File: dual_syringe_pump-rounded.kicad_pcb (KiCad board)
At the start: 2 copper layers, 100.3 x 85.5 mm, 163 parts, among them J2 Barrel_Jack_Switch_Pin3Ring, Q1 SS8050, Q2 SS8050, Q3 SS8050, Q4 SS8050, U1 ESP32-WROOM-32, U2 AMS1117-3.3, U3 CH340C, U4 TP5100, U5 LM2596S-buck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

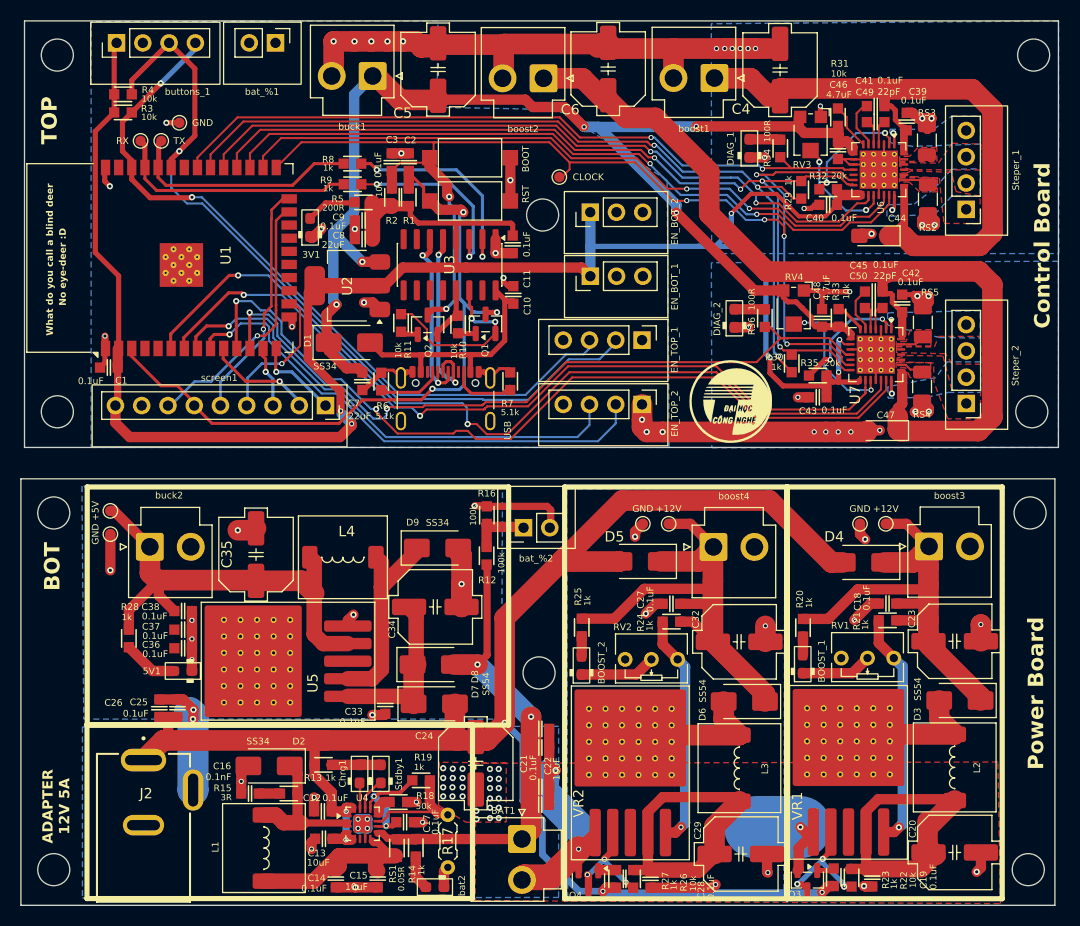
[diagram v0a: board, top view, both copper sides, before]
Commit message: Highlighted connectors
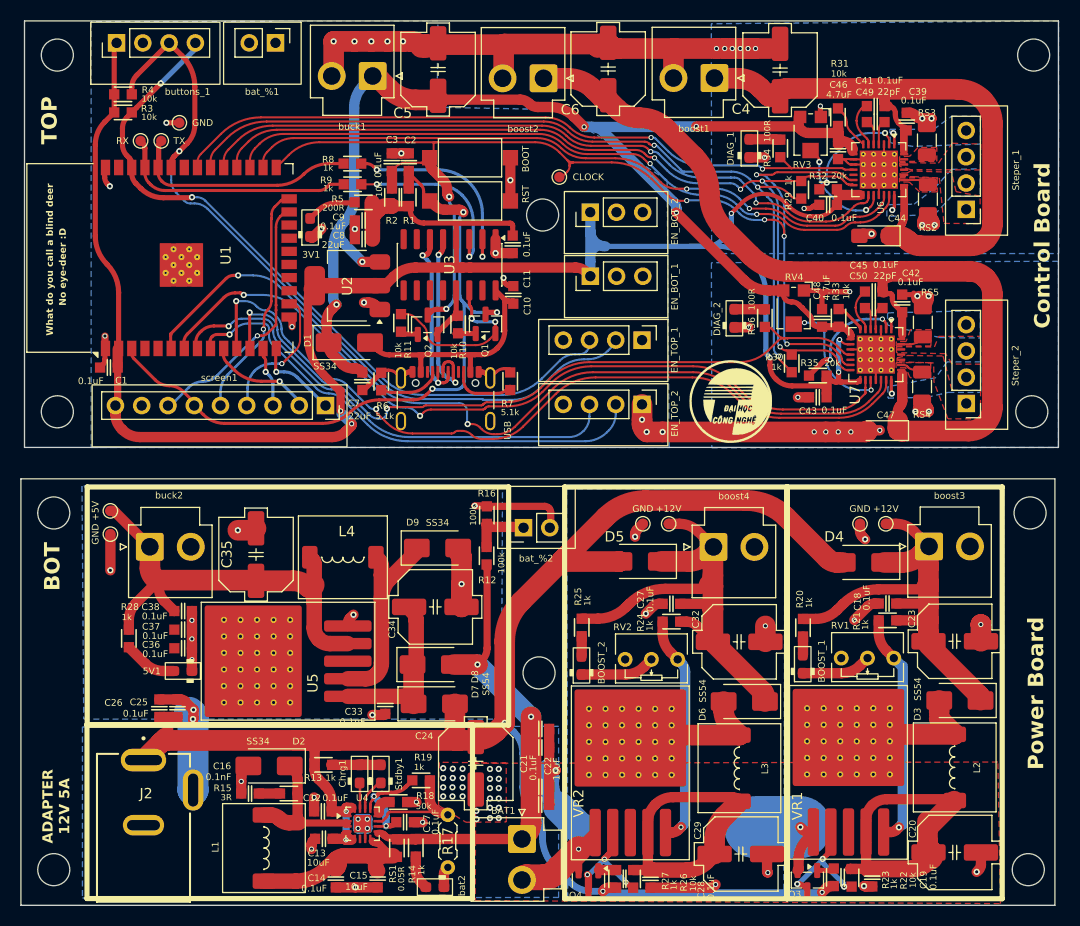
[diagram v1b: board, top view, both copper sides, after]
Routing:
- net GND1: track 164.3 -> 161.6 mm
- net EN_2: track 80.2 -> 78.1 mm
- net Net-(D9-K): track 19.5 -> 21.5 mm
- net DIR_2: track 85.7 -> 83.9 mm
- net +12V_2: track 138.0 -> 136.1 mm
- net STEP_2: track 79.3 -> 77.6 mm
- net EN_1: track 69.8 -> 68.2 mm
- net DIR_1: track 67.2 -> 65.6 mm
- net Net-(Q4-C): track 12.2 -> 10.6 mm
- net DIAG_2: track 73.6 -> 72.1 mm
- net STEP_1: track 70.5 -> 69.0 mm
- net /SDA: track 78.4 -> 76.9 mm
- net RX_TMC: track 90.0 -> 88.5 mm
- net +5V: track 171.3 -> 172.7 mm
- net Adapter_+12V: track 186.5 -> 185.1 mm
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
